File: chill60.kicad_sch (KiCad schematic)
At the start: 7 parts, among them J1 Molex_Pico-EZmate_78171-0004_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, SW1 RST, SW2 BOOT, U1 STM32F072CBTx, U2 XC6206PxxxMR

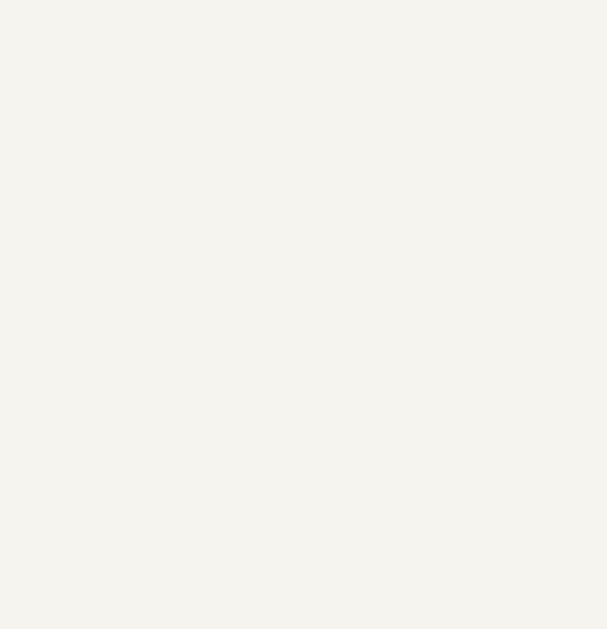
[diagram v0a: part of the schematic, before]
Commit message: add switch diode matrix
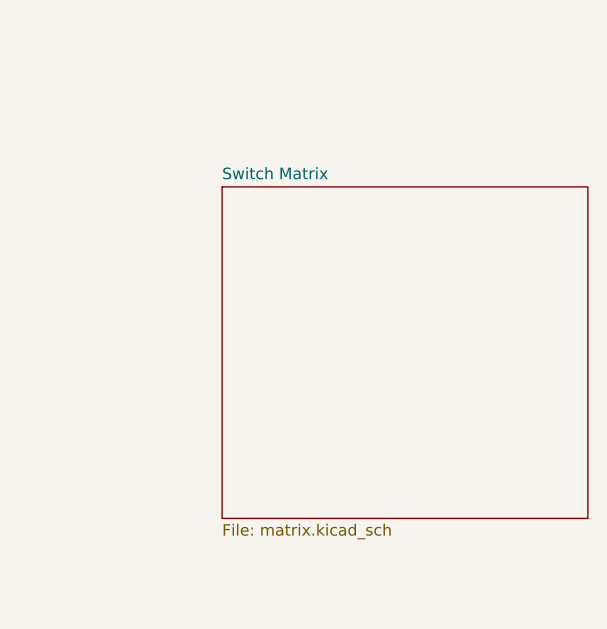
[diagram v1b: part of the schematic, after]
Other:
- added sheet Switch Matrix (matrix.kicad_sch)
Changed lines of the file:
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@@
+    )
+  )
+  (sheet (at 196.85 97.79) (size 40.64 36.83) (fields_autoplaced)
+    (stroke (width 0.1524) (type solid))
+    (fill (color 0 0 0 0.0000))
+    (property "Sheetname" "Switch Matrix" (at 196.85 97.0784 0)
+      (effects (font (size 1.27 1.27)) (justify left bottom))
+    )
+    (property "Sheetfile" "matrix.kicad_sch" (at 196.85 135.2046 0)
+      (effects (font (size 1.27 1.27)) (justify left top))
+    )
+    (instances
+      (project "chill60"
+        (path "/98d602aa-46a9-4e45-be3d-3b1e6175f1d0" (page "2"))
+      )
     )
   )

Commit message: initial complete schematic
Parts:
- added C10, C9: 4.7u, symbol Device:C_Small
- added C11, C2, C3: 1u, symbol Device:C_Small
- added C4, C5, C6, C7: 100n, symbol Device:C_Small
- added C8: 10n, symbol Device:C_Small
- added D67: LED, marbastlib-mx:LED_MX_3mm, symbol Device:LED
- added D68: LED, marbastlib-mx:LED_MX_3mm-FLIPPED, symbol Device:LED
- added R2, R3: 27, symbol Device:R_Small
- added R6: 470R, Resistor_SMD:R_0402_1005Metric, symbol Device:R_Small
- C1: value C_Small -> 100n
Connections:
- net +3V3: now also U1.1 (VBAT), U1.24 (VDD), U1.36 (VDDIO2), U1.48 (VDD), U1.9 (VDDA), U2.2 (VO), C10.1, C11.1, C3.1, C4.1, C5.1, C6.1, C7.1, C8.1, C9.1, D67.2 (A), D68.2 (A)
- net +5V: now also U2.3 (VI), C2.1
- net D+: now also R3.2; no longer U1.33 (PA12)
- net D-: now also R2.2; no longer U1.32 (PA11)
- net GND: now also U2.1 (GND), C10.2, C11.2, C2.2, C3.2, C4.2, C5.2, C6.2, C7.2, C8.2, C9.2
- net NRST renamed ~{RST}
- new net: R2.1, U1.32 (PA11)
- new net: D67.1 (K), D68.1 (K), R6.2
- new net: R3.1, U1.33 (PA12)
- new net CAPSLCK: R6.1
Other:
- note removed: "TODO: decoupling"
- moved on the sheet: J1, U2

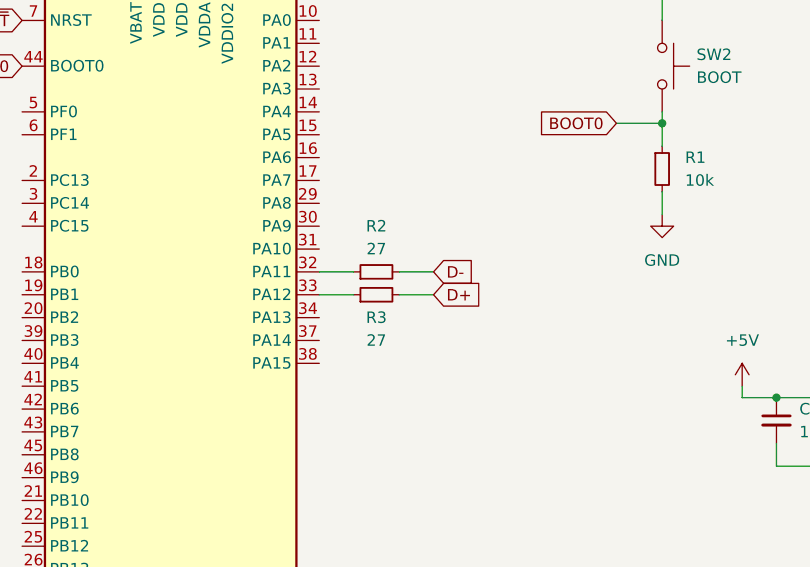
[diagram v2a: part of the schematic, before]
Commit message: remove USB terminating resistors (not needed)
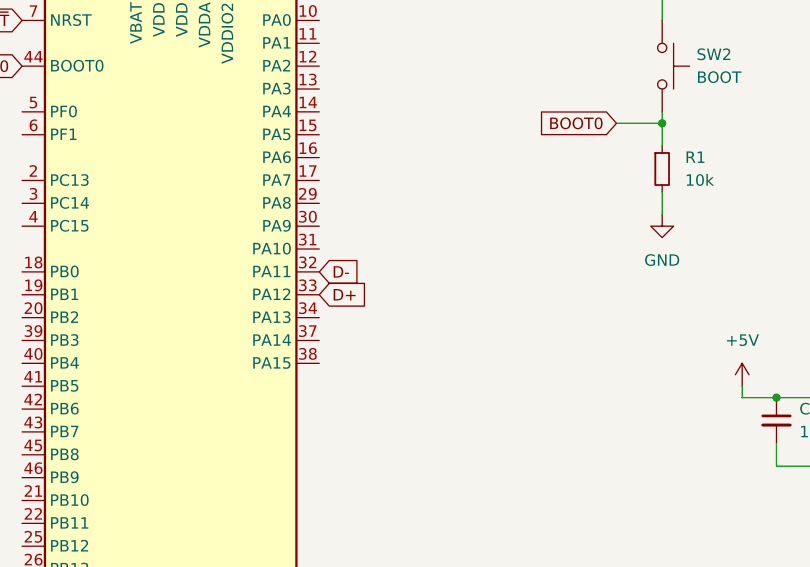
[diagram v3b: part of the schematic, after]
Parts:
- removed R2, R3: 27, symbol Device:R_Small
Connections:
- net D+: now also U1.33 (PA12)
- net D-: now also U1.32 (PA11)
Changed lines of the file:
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@@
-    (stroke (width 0) (type default))
-  )
-  (wire (pts (xy 55.88 85.09) (xy 59.69 85.09))
     (stroke (width 0) (type default))
   )
@@
     (stroke (width 0) (type default))
   )
-  (wire (pts (xy 64.77 87.63) (xy 68.58 87.63))
-    (stroke (width 0) (type default))
-  )
   (wire (pts (xy 123.19 130.81) (xy 133.35 130.81))
     (stroke (width 0) (type default))
@@
     (stroke (width 0) (type default))
   )
-  (wire (pts (xy 64.77 85.09) (xy 68.58 85.09))
-    (stroke (width 0) (type default))
-  )
   (wire (pts (xy 91.44 130.81) (xy 101.6 130.81))
     (stroke (width 0) (type default))
@@
   )
   (wire (pts (xy 143.51 125.73) (xy 153.67 125.73))
-    (stroke (width 0) (type default))
-  )
-  (wire (pts (xy 55.88 87.63) (xy 59.69 87.63))
     (stroke (width 0) (type default))
   )
@@
     )
   )
-  (global_label "D+" (shape input) (at 68.58 87.63 0) (fields_autoplaced)
+  (global_label "D+" (shape input) (at 55.88 87.63 0) (fields_autoplaced)
     (effects (font (size 1.27 1.27)) (justify left))
-    (property "Intersheetrefs" "${INTERSHEET_REFS}" (at 74.4076 87.63 0)
+    (property "Intersheetrefs" "${INTERSHEET_REFS}" (at 61.7076 87.63 0)
       (effects (font (size 1.27 1.27)) (justify left) hide)
     )
@@
     )
   )
-  (global_label "D-" (shape input) (at 68.58 85.09 0) (fields_autoplaced)
+  (global_label "D-" (shape input) (at 55.88 85.09 0) (fields_autoplaced)
     (effects (font (size 1.27 1.27)) (justify left))
-    (property "Intersheetrefs" "${INTERSHEET_REFS}" (at 74.4076 85.09 0)
+    (property "Intersheetrefs" "${INTERSHEET_REFS}" (at 61.7076 85.09 0)
       (effects (font (size 1.27 1.27)) (justify left) hide)
     )
@@
         (path "/98d602aa-46a9-4e45-be3d-3b1e6175f1d0"
           (reference "#PWR07") (unit 1)
-        )
-      )
-    )
-  )
-  (symbol (lib_id "Device:R_Small") (at 62.23 85.09 90) (unit 1)
-    (in_bom yes) (on_board yes) (dnp no) (fields_autoplaced)
-    (property "Reference" "R2" (at 62.23 80.01 90)
-      (effects (font (size 1.27 1.27)))
-    )
-    (property "Value" "27" (at 62.23 82.55 90)
-      (effects (font (size 1.27 1.27)))
-    )
-    (property "Footprint" "" (at 62.23 85.09 0)
-      (effects (font (size 1.27 1.27)) hide)
-    )
-    (property "Datasheet" "~" (at 62.23 85.09 0)
-      (effects (font (size 1.27 1.27)) hide)
-    )
-    (pin "1")
-    (pin "2")
-    (instances
-      (project "chill60"
-        (path "/98d602aa-46a9-4e45-be3d-3b1e6175f1d0"
-          (reference "R2") (unit 1)
         )
       )
@@
         )
       )
-    )
-  )
-  (symbol (lib_id "Device:R_Small") (at 62.23 87.63 90) (unit 1)
-    (in_bom yes) (on_board yes) (dnp no)
-    (property "Reference" "R3" (at 62.23 90.17 90)
-      (effects (font (size 1.27 1.27)))
-    )
-    (property "Value" "27" (at 62.23 92.71 90)
-      (effects (font (size 1.27 1.27)))
-    )
-    (property "Footprint" "" (at 62.23 87.63 0)
-      (effects (font (size 1.27 1.27)) hide)
-    )
-    (property "Datasheet" "~" (at 62.23 87.63 0)
-      (effects (font (size 1.27 1.27)) hide)
-    )
-    (pin "1")
-    (pin "2")
-    (instances
-      (project "chill60"
-        (path "/98d602aa-46a9-4e45-be3d-3b1e6175f1d0"
-          (reference "R3") (unit 1)
-        )
-      )

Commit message: add PCB
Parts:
- removed C10: 4.7u, symbol Device:C_Small
- C1, C2, C3: footprint (none) -> Capacitor_SMD:C_0402_1005Metric
- C10: renamed from C11; footprint (none) -> Capacitor_SMD:C_0402_1005Metric
- C4: renamed from C9; footprint (none) -> Capacitor_SMD:C_0402_1005Metric
- C5: renamed from C4; footprint (none) -> Capacitor_SMD:C_0402_1005Metric
- C6: renamed from C5; footprint (none) -> Capacitor_SMD:C_0402_1005Metric
- C7: renamed from C6; footprint (none) -> Capacitor_SMD:C_0402_1005Metric
- C8: renamed from C7; footprint (none) -> Capacitor_SMD:C_0402_1005Metric
- C9: renamed from C8; footprint (none) -> Capacitor_SMD:C_0402_1005Metric
- D68: footprint marbastlib-mx:LED_MX_3mm-FLIPPED -> marbastlib-mx:LED_MX_3mm-ROT
- R1: footprint (none) -> Resistor_SMD:R_0603_1608Metric
- SW1, SW2: footprint (none) -> Button_Switch_SMD:SW_SPST_TL3342
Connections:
- net +3V3: now also R6.2; no longer D67.2 (A), D68.2 (A)
- net CAPSLCK: now also D67.1 (K), D68.1 (K), U1.25 (PB12); no longer R6.1
- net ROW2: now reaches U1.10 (PA0)
- net COL13: now reaches U1.11 (PA1)
- net COL12: now reaches U1.12 (PA2)
- net COL11: now reaches U1.13 (PA3)
- net COL10: now reaches U1.14 (PA4)
- net COL09: now reaches U1.15 (PA5)
- net COL08: now reaches U1.16 (PA6)
- net COL07: now reaches U1.17 (PA7)
- net COL06: now reaches U1.18 (PB0)
- net COL05: now reaches U1.19 (PB1)
- net COL04: now reaches U1.20 (PB2)
- net COL03: now reaches U1.21 (PB10)
- net COL02: now reaches U1.22 (PB11)
- net COL00: now reaches U1.26 (PB13)
- net ROW3: now reaches U1.27 (PB14)
- net ROW4: now reaches U1.28 (PB15)
- net ROW0: now reaches U1.30 (PA9)
- net ROW1: now reaches U1.31 (PA10)
- net COL01: now reaches U1.45 (PB8)
- new net: D67.2 (A), D68.2 (A), R6.1
- no-connect marks 0 -> 7
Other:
- moved on the sheet: C10, C4, R6, U1
